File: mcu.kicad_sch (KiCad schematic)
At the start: 11 parts, among them J1 USB4105-GF-A, Q2 BC847BDW1, U1 ESP32-C6-MINI-1, U4 FT231XQ

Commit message: added switched
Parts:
- added BOOT, RST: SW_Push, symbol Switch:SW_Push
- added C32, C34: 0.1u, symbol Device:C
- added C33: 1u, symbol Device:C
- added R12: 10k, symbol Device:R_US
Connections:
- net 3V3: now also R12.1
- net CHIP_PU: now also U1.8 (EN), C32.1, C33.2, R12.2, RST.2
- net GND: now also BOOT.1, C32.2, C33.1, C34.2, RST.1
- net IO9: now also U1.23 (IO9)
- net IO0: now reaches U1.12 (IO0)
- net IO0: now also BOOT.2, C34.1
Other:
- moved on the sheet: C31, J1, Q2A, Q2B, R10, R11, R6, R7, R8, R9, U1, U4

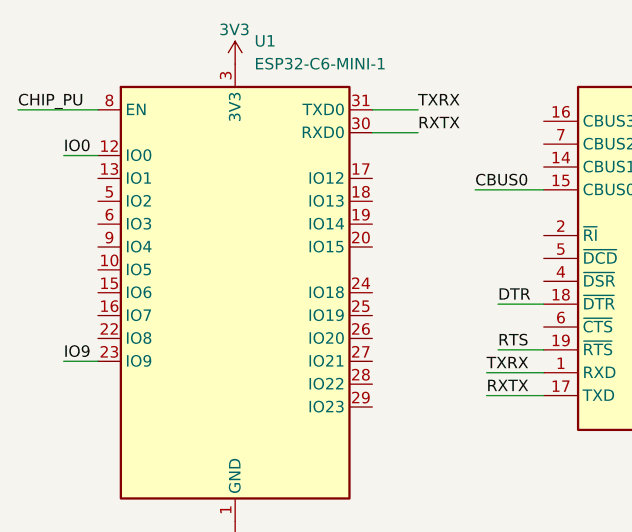
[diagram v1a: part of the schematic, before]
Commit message: added radio receiver control
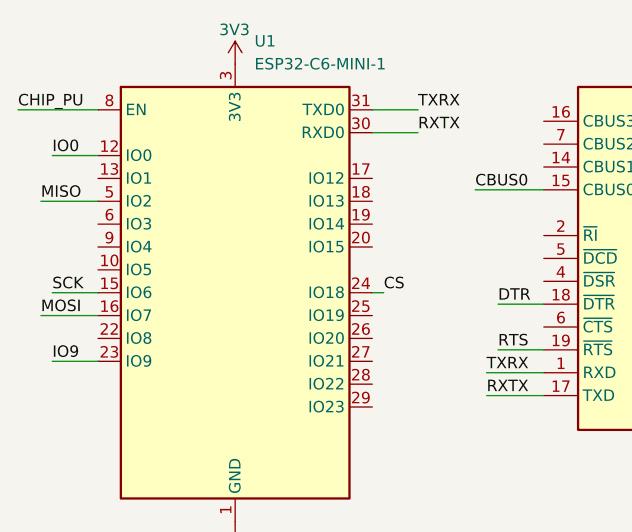
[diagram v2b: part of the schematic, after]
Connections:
- net SCK: now reaches U1.15 (IO6)
- net MOSI: now reaches U1.16 (IO7)
- net CS: now reaches U1.24 (IO18)
- net MISO: now reaches U1.5 (IO2)
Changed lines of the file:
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@@
+	(wire
+		(pts
+			(xy 110.49 45.72) (xy 116.84 45.72)
+		)
+		(stroke
+			(width 0)
+			(type default)
+		)
+	)
 	(wire
 		(pts
@@
 	(wire
 		(pts
-			(xy 113.03 27.94) (xy 116.84 27.94)
+			(xy 111.76 27.94) (xy 116.84 27.94)
 		)
 		(stroke
@@
 	(wire
 		(pts
+			(xy 111.76 43.18) (xy 116.84 43.18)
+		)
+		(stroke
+			(width 0)
+			(type default)
+		)
+	)
+	(wire
+		(pts
 			(xy 222.25 30.48) (xy 226.06 30.48)
 		)
@@
 	(wire
 		(pts
-			(xy 113.03 50.8) (xy 116.84 50.8)
+			(xy 111.76 50.8) (xy 116.84 50.8)
 		)
 		(stroke
@@
 	(wire
 		(pts
+			(xy 110.49 33.02) (xy 116.84 33.02)
+		)
+		(stroke
+			(width 0)
+			(type default)
+		)
+	)
+	(wire
+		(pts
 			(xy 170.18 97.79) (xy 171.45 97.79)
 		)
@@
 	(wire
 		(pts
+			(xy 147.32 43.18) (xy 148.59 43.18)
+		)
+		(stroke
+			(width 0)
+			(type default)
+		)
+	)
+	(wire
+		(pts
 			(xy 160.02 52.07) (xy 166.37 52.07)
 		)
@@
 			(width 0)
 			(type default)
+		)
+	)
+	(label "CS"
+		(at 148.59 43.18 0)
+		(effects
+			(font
+				(size 1.27 1.27)
+			)
+			(justify left bottom)
 		)
 	)
@@
 		)
 	)
+	(label "SCK"
+		(at 111.76 43.18 0)
+		(effects
+			(font
+				(size 1.27 1.27)
+			)
+			(justify left bottom)
+		)
+	)
 	(label "C31"
 		(at 205.74 54.61 0)
@@
 	)
 	(label "IO9"
-		(at 113.03 50.8 0)
+		(at 111.76 50.8 0)
+		(effects
+			(font
+				(size 1.27 1.27)
+			)
+			(justify left bottom)
+		)
+	)
+	(label "MOSI"
+		(at 110.49 45.72 0)
 		(effects
 			(font
@@
 		)
 	)
+	(label "MISO"
+		(at 110.49 33.02 0)
+		(effects
+			(font
+				(size 1.27 1.27)
+			)
+			(justify left bottom)
+		)
+	)
 	(label "CHIP_PU"
 		(at 186.69 97.79 0)
@@
 	)
 	(label "IO0"
-		(at 113.03 27.94 0)
-		(effects
-			(font
+		(at 111.76 27.94 0)
+		(effects
+			(font
